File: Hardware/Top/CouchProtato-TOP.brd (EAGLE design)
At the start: 38 x 38 mm, 52 parts, among them SW1 SWITCH.MOM, SW2 SWITCH.MOM, SW5 SWITCH.MOM, U2 NRF52832_MODULE_MDBT42, U4 PCF8523

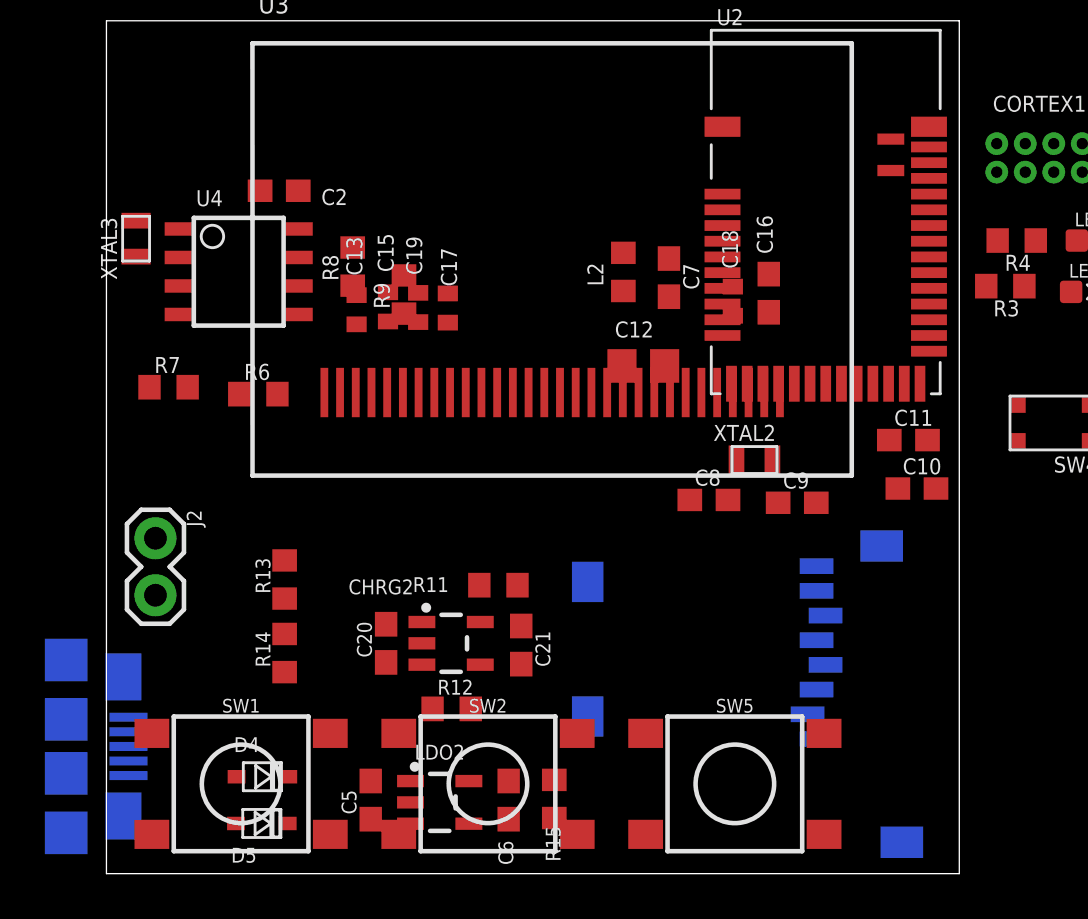
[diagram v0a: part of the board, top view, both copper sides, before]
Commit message: Top schematic finished
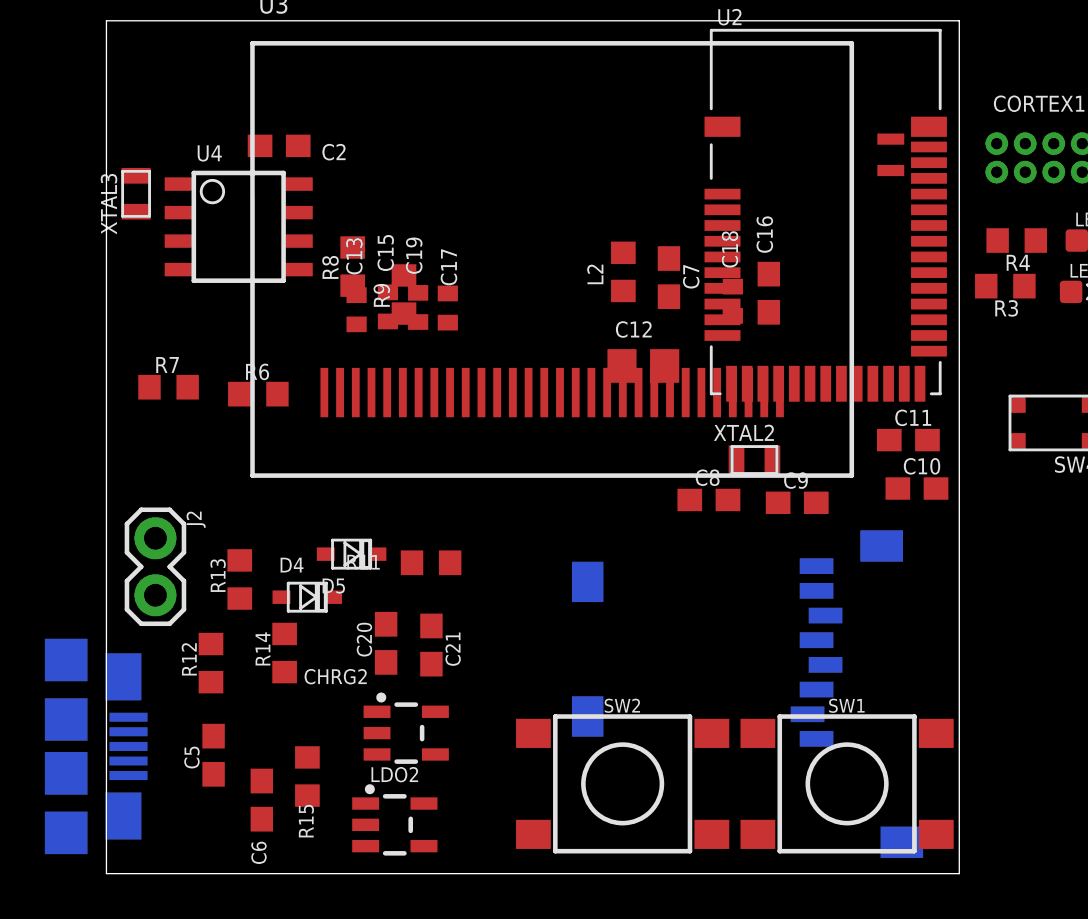
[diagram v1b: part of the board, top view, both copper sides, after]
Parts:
- removed SW5: SWITCH.MOM, LinnesLab-Switches:TACTILE_SWITCH_SMD_6.2MM_TALL
- moved SW1 27.0 mm to (33.0, 4.00)
- moved D5 12.6 mm to (10.9, 14.2)
- moved R15 11.0 mm to (8.95, 4.33)
- moved C6 11.0 mm to (6.92, 3.28)
- moved R12 10.9 mm to (4.66, 9.38), turned to 90 degrees
- moved D4 8.25 mm to (8.95, 12.3)
- moved C5 7.28 mm to (4.78, 5.28)
- moved SW2 6.00 mm to (23.0, 4.00)
- moved CHRG2 4.47 mm to (13.4, 6.26)
- moved C21 4.00 mm to (14.5, 10.2)
- moved R11 3.16 mm to (14.5, 13.9)
- moved LDO2 2.24 mm to (12.8, 2.17)
- moved C2 2.00 mm to (7.70, 32.4)
- moved R13 2.00 mm to (5.94, 13.1)
- moved U4 2.00 mm to (5.89, 28.8)
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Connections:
- net VBATT renamed VBAT
- removed net N$16: SW1.A1
- removed net N$18: SW1.B1, SW1.B2
- removed net N$21: SW2.A1
- removed net N$22: SW2.B1, SW2.B2
- removed net N$23: SW5.A1
- removed net N$24: SW5.B1, SW5.B2
- new net SW1: SW1.A1, SW2.A1
- net GND: now also SW1.B1, SW1.B2, SW2.B1, SW2.B2, USB2.S1, USB2.S2, USB2.S3, USB2.S4, USB2.S5, USB2.S6

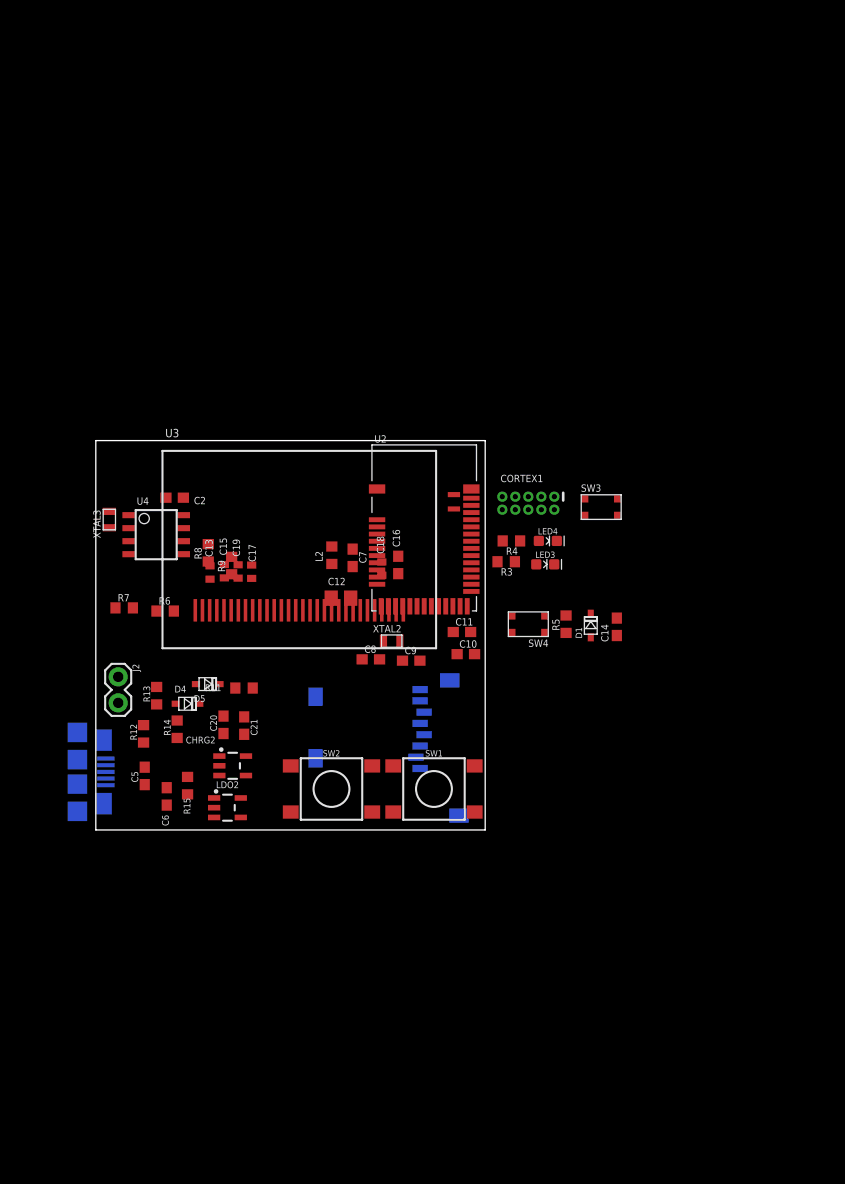
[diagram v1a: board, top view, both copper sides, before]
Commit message: Finished routing top and bottom boards
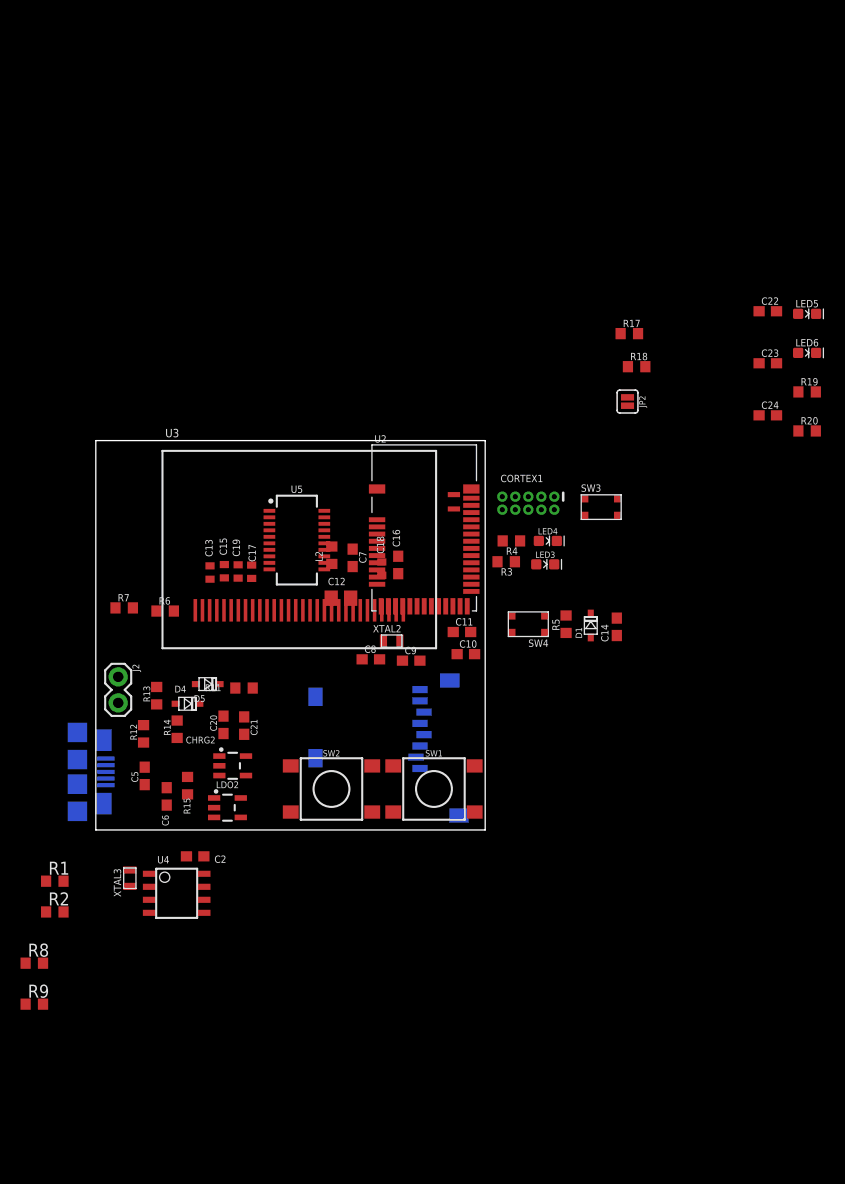
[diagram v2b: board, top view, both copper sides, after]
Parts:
- added C22: 100n, LinnesLab-Passives:C0603
- added C23, C24: 47p, LinnesLab-Passives:C0603
- added JP2: (no value), LinnesLab-Switches:SMT-JUMPER_2_NO_SILK
- added LED5: RED, LinnesLab-LED:LED-0603
- added LED6: YELLOW, LinnesLab-LED:LED-0603
- added R1, R2: 0, LinnesLab-Passives:R0603
- added R17, R18: 27, LinnesLab-Passives:R0603
- added R19, R20: 1k, LinnesLab-Passives:R0603
- added U5: FT231XS, LinnesLab-DigitalIC:SSOP20_L
- moved R9 46.9 mm to (-6.00, -17.0), turned to 0 degrees
- moved R8 43.5 mm to (-6.00, -13.0), turned to 0 degrees
- moved C2 35.1 mm to (9.70, -2.57)
- moved U4 35.1 mm to (7.89, -6.18)
- moved XTAL3 35.1 mm to (3.32, -4.71)
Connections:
- removed net BATT: R13.1, R14.2
- removed net CD1: SD2.CD1
- removed net CHRG.STAT: CHRG2.1, R12.1
- removed net CS.OLED: U3.13
- removed net DC.OLED: U3.15
- removed net RESET.OLED: U3.14
- removed net RXD: U2.21
- removed net SD.CS: SD2.2
- removed net SW1: SW1.A1, SW2.A1
- removed net TXD: U2.19
- new net !CTS: JP2.2, U5.9
- new net !DTR: U5.1
- new net A4/BATT: R13.1, R14.2, U2.5
- new net A6/TIA: U2.7
- new net A7/PPG: U2.8
- new net D11/SW1: SW1.A1, U2.25
- new net D15/SW2: SW2.A1, U2.29
- new net D16/CS.OLED: U2.30, U3.13
- new net D27/CHRG.STATUS: CHRG2.1, R12.1, U2.4
- new net D29/LED.CTRL: U2.6
- new net D3/RESET.OLED: U2.16, U3.14
- new net D4/DC.OLED: U2.17, U3.15
- new net D5/CD1: SD2.CD1, U2.18
- new net D7/SD.CS: SD2.2, U2.20
- new net FT3V3: U5.13
- new net N$23: R17.2, U5.12
- new net N$24: R18.2, U5.11
- new net N$25: LED5.C, R19.2
- new net N$26: LED6.C, R20.2
- new net RXD.NRF: R1.2, U2.21
- new net RXDFT: R2.1, U5.4
- new net RXLED: R19.1, U5.17
- new net TXD.NRF: R2.2, U2.19
- new net TXDFT: R1.1, U5.20
- new net TXLED: R20.1, U5.10
- net 3.3V: now also C22.2, LED5.A, LED6.A, U5.14, U5.3
- net GND: now also C22.1, C23.2, C24.1, JP2.1, U5.16, U5.6
- net SCL: now also R9.1; no longer R8.1
- net SDA: now also R8.1; no longer R9.1
- net USB+: now also C23.1, R18.1
- net USB-: now also C24.2, R17.1
- net V_USB: now also U5.15

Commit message: finished routing bottom board and began top. finished take 003.
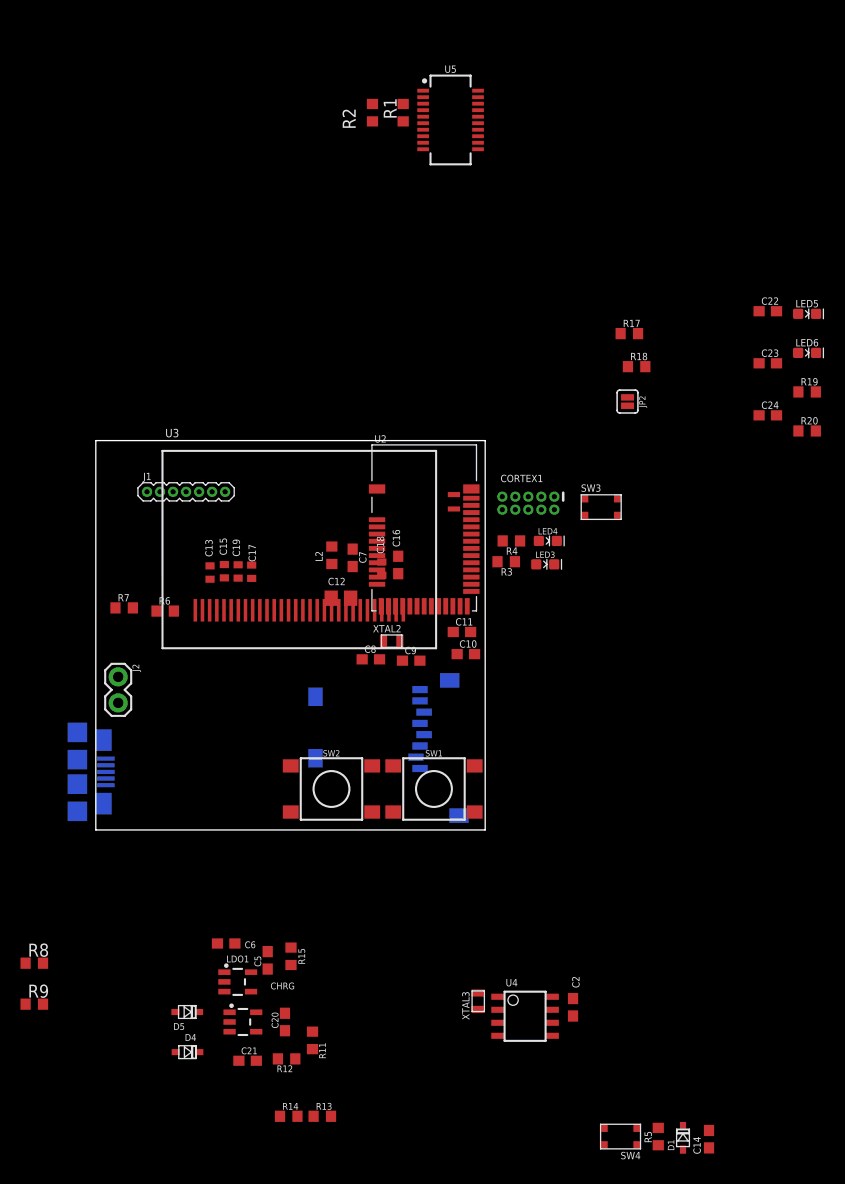
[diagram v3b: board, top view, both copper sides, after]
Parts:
- removed CHRG2: MCP73831, LinnesLab-Power:SOT23-5
- removed LDO2: MIC5504, LinnesLab-Power:SOT23-5
- added CHRG: MCP73831, LinnesLab-Power:SOT23-5
- added J1: (no value), LinnesLab-Connectors:1X07_1.27MM
- added LDO1: MIC5504, LinnesLab-Power:SOT23-5
- moved R2 83.9 mm to (27.0, 70.0), turned to 90 degrees
- moved R1 82.3 mm to (30.0, 70.0), turned to 90 degrees
- moved C14 50.8 mm to (59.8, -30.2)
- moved D1 50.8 mm to (57.3, -30.0)
- moved R5 50.8 mm to (54.9, -29.9)
- moved SW4 50.8 mm to (51.2, -29.9)
- moved R13 44.1 mm to (22.1, -27.9), turned to 0 degrees
- moved U5 43.7 mm to (34.6, 69.3)
- moved C2 39.7 mm to (46.6, -17.3), turned to 270 degrees
- moved R14 39.3 mm to (18.8, -27.9), turned to 0 degrees
- moved XTAL3 36.1 mm to (37.3, -16.7)
- moved U4 36.1 mm to (41.9, -18.2)
- moved R11 35.0 mm to (21.1, -20.5), turned to 270 degrees
- moved R12 34.7 mm to (18.6, -22.3), turned to 180 degrees
- moved D4 34.0 mm to (8.95, -21.7)
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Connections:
- net 3.3V: now also J1.4, LDO1.5; no longer LDO2.5
- net A6/TIA: now also J1.6
- net A7/PPG: now also J1.7
- net D27/CHRG.STATUS: now also CHRG.1; no longer CHRG2.1
- net D29/LED.CTRL: now also J1.5
- net GND: now also CHRG.2, J1.3, LDO1.2; no longer CHRG2.2, LDO2.2
- net N$17: now also CHRG.5; no longer CHRG2.5
- net SCL: now also J1.2
- net SDA: now also J1.1
- net VIN: now also CHRG.4, LDO1.1, LDO1.3; no longer CHRG2.4, LDO2.1, LDO2.3
- net VLIPO: now also CHRG.3; no longer CHRG2.3

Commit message: In the middle of routing top board, working on OLED
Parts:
- moved R20 44.7 mm to (40.4, 72.9)
- moved C22 41.5 mm to (29.6, 71.4), turned to 270 degrees
- moved R19 40.3 mm to (40.4, 70.7)
- moved LED6 36.6 mm to (44.6, 73.4), turned to 180 degrees
- moved C24 35.6 mm to (43.5, 68.4), turned to 270 degrees
- moved LED5 32.0 mm to (44.6, 70.6), turned to 180 degrees
- moved C23 29.0 mm to (43.5, 64.4), turned to 270 degrees
- moved C10 28.9 mm to (64.1, 10.2)
- moved C11 28.9 mm to (63.7, 12.3)
- moved C8 26.9 mm to (52.8, 9.65)
- moved C9 26.7 mm to (56.8, 10.5)
- moved XTAL2 26.7 mm to (54.9, 12.4)
- moved JP2 23.6 mm to (37.9, 60.8)
- moved R18 23.6 mm to (41.2, 65.8), turned to 180 degrees
- moved R17 22.1 mm to (40.9, 67.6), turned to 180 degrees
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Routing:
- net TXLED: track 0.00 -> 12.5 mm, vias 0 -> 2
- net RXDFT: track 0.00 -> 8.68 mm
- net N$12: track 0.00 -> 8.06 mm
- net N$5: track 0.00 -> 4.88 mm
- net N$11: track 0.00 -> 4.76 mm
- net N$8: track 0.00 -> 4.69 mm
- net TXDFT: track 0.00 -> 3.92 mm
- net GND: track 0.00 -> 3.86 mm, vias 0 -> 4
- net N$24: track 0.00 -> 3.34 mm
- net N$23: track 0.00 -> 2.99 mm
- net N$3: track 0.00 -> 2.89 mm
- net N$26: track 0.00 -> 2.65 mm
- net N$7: track 0.00 -> 2.55 mm
- net N$25: track 0.00 -> 2.49 mm
- net RXLED: track 0.00 -> 2.48 mm
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- added copper zone on layer 1, net 3.3V
- added copper zone on layer 16, net GND

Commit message: 22.42 through take 3, continued routing top board
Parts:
- moved R7 24.6 mm to (33.8, 19.9)
- moved C18 15.3 mm to (32.8, 21.9), turned to 180 degrees
- moved R6 9.82 mm to (17.2, 24.5), turned to 270 degrees
- moved C16 4.30 mm to (23.5, 24.2), turned to 0 degrees
- moved C12 4.16 mm to (20.8, 29.2), turned to 270 degrees
- moved L2 1.35 mm to (23.7, 28.7)
- moved U2 1.33 mm to (31.3, 31.2)
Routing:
- net GND: track 3.86 -> 16.0 mm, vias 4 -> 11
- net N$2: track 0.00 -> 8.53 mm
- net N$15: track 0.00 -> 7.56 mm
- net N$1: track 0.00 -> 2.39 mm
- net N$11: track 4.76 -> 3.68 mm
